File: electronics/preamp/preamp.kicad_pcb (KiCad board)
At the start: 2 copper layers, 25 x 25 mm, 28 parts, among them J1 Conn_01x01, J2 Conn_01x01, J3 Conn_01x05, U1 TL064

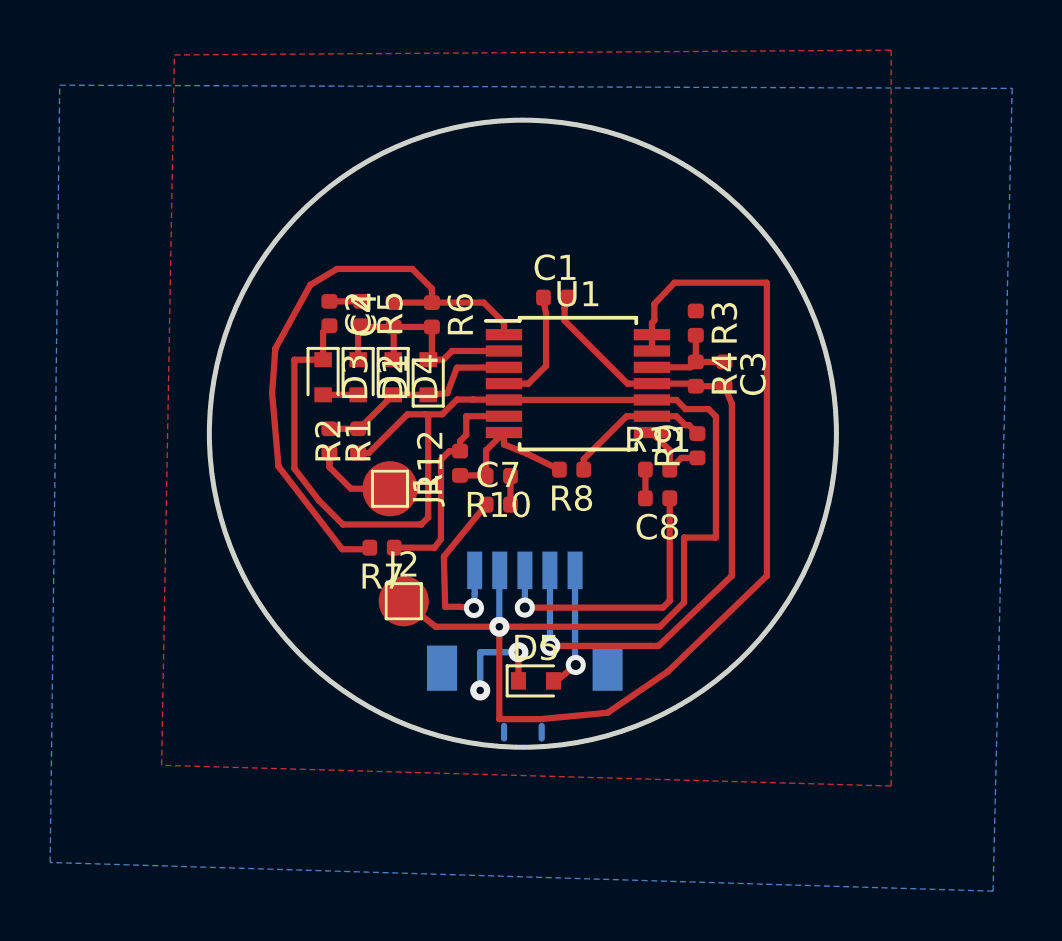
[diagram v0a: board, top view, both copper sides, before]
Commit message: Compress and prettify traces
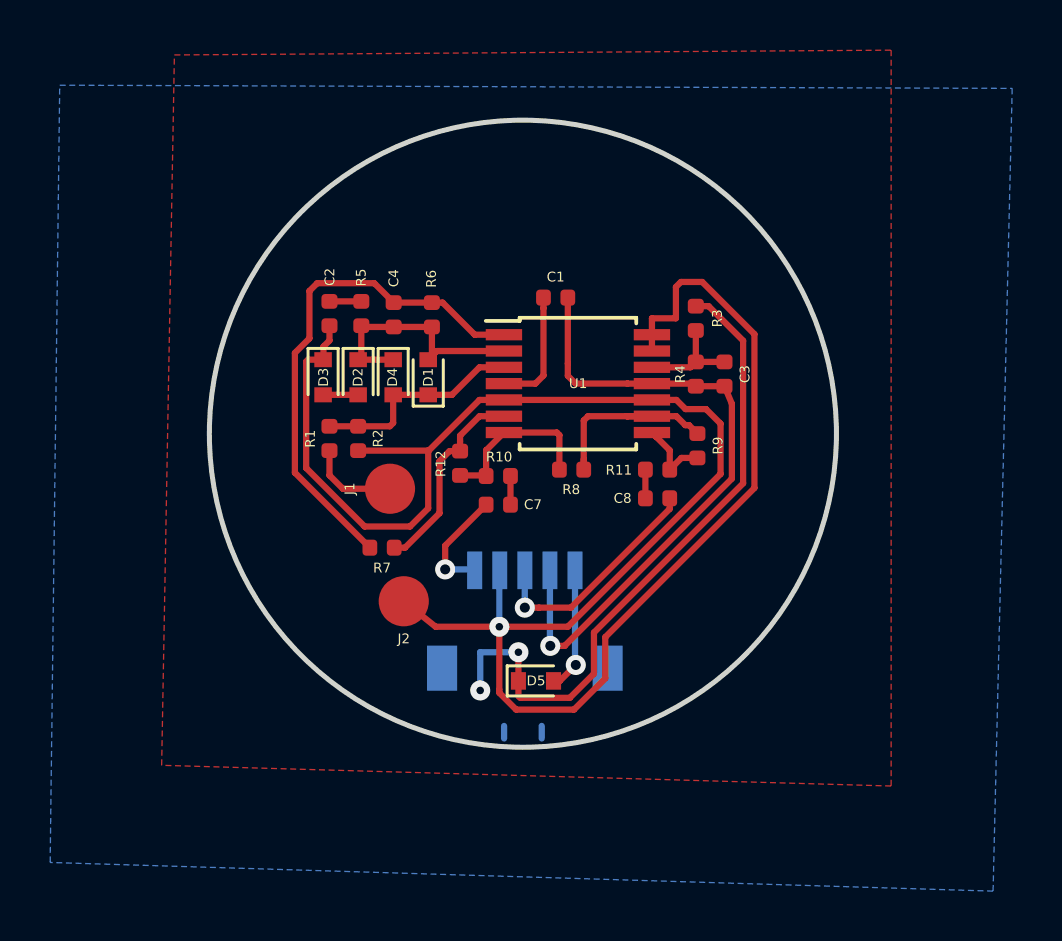
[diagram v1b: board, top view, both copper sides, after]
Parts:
- R9: value 100k 1% -> 100k 1%
- moved R3 0.19 mm to (106.9, 95.4)
- moved R1 0.10 mm to (92.3, 100.2)
- moved R2 0.10 mm to (93.4, 100.2)
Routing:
- net VCC: track 9.00 -> 31.3 mm
- net VGND: track 90.6 -> 81.7 mm
- net /AMP: track 24.0 -> 20.6 mm
- net /OUT+: track 7.38 -> 4.45 mm
- net /INV-: track 5.95 -> 8.28 mm
- net /OUT-: track 11.5 -> 9.32 mm
- net -BATT: track 27.6 -> 26.4 mm
- net /GAIN-: track 9.10 -> 8.12 mm
- net /BUF+: track 5.98 -> 6.71 mm
- net /IN+: track 4.08 -> 3.52 mm

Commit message: preamp: Use via shield
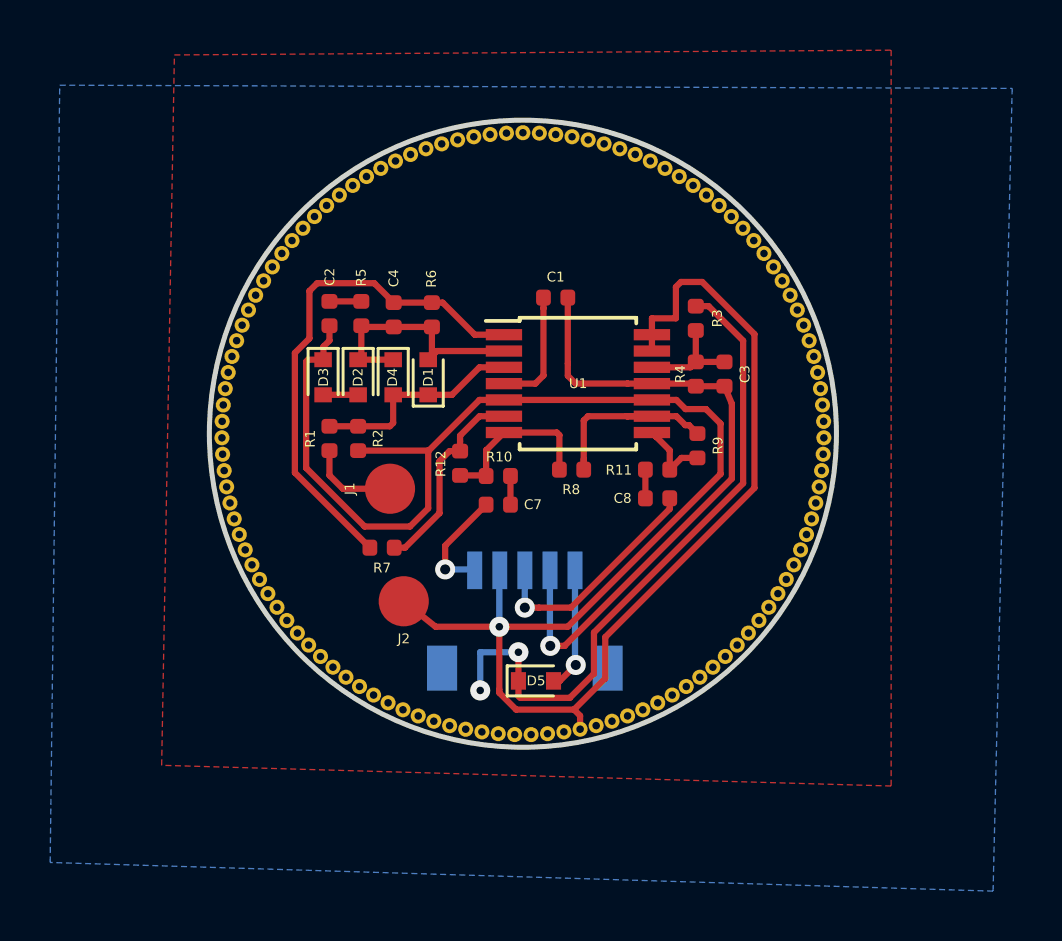
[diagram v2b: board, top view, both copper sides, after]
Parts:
- added J4: Conn_01x01, piezopro:viashield, B.Cu at (100.0, 100.0)
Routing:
- net (no net): track 1.00 -> 0.00 mm
- net VGND: track 81.7 -> 82.6 mm

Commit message: preamp: Move last via underneath connector
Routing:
- net /OUT+: track 4.45 -> 7.40 mm
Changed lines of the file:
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@@
     (thickness 1.6)
     (drawings 65)
-    (tracks 179)
+    (tracks 182)
     (zones 0)
     (modules 29)
@@
   (segment (start 102.280769 111.243357) (end 102.280769 111.78126) (width 0.25) (layer F.Cu) (net 3))
   (segment (start 102.037412 111) (end 102.280769 111.243357) (width 0.25) (layer F.Cu) (net 3))
-  (via (at 96.901 105.41) (size 0.8) (drill 0.4) (layers F.Cu B.Cu) (net 4))
+  (via (at 98.044 106.934) (size 0.8) (drill 0.4) (layers F.Cu B.Cu) (net 4))
   (segment (start 98.041 105.41) (end 98.078 105.447) (width 0.25) (layer B.Cu) (net 4))
-  (segment (start 96.901 105.41) (end 98.041 105.41) (width 0.25) (layer B.Cu) (net 4))
-  (segment (start 96.901 104.46272) (end 96.901 105.41) (width 0.25) (layer F.Cu) (net 4))
   (segment (start 98.53436 102.82936) (end 96.901 104.46272) (width 0.25) (layer F.Cu) (net 4))
+  (segment (start 98.044 106.934) (end 97.028 106.934) (width 0.25) (layer F.Cu) (net 4))
+  (segment (start 96.901 106.807) (end 97.028 106.934) (width 0.25) (layer F.Cu) (net 4))
+  (segment (start 96.901 104.46272) (end 96.901 106.807) (width 0.25) (layer F.Cu) (net 4))
+  (segment (start 98.044 105.481) (end 98.078 105.447) (width 0.25) (layer B.Cu) (net 4))
+  (segment (start 98.044 106.934) (end 98.044 105.481) (width 0.25) (layer B.Cu) (net 4))
   (segment (start 99.50436 101.68636) (end 99.50436 102.82936) (width 0.25) (layer F.Cu) (net 5))
   (segment (start 104.88436 101.43236) (end 104.88436 102.57536) (width 0.25) (layer F.Cu) (net 6))
@@
   )
   (zone (net 3) (net_name VGND) (layer B.Cu) (hatch edge 0.508)
-    (connect_pads (clearance -0.2))
+    (connect_pads yes (clearance -0.2))
     (min_thickness 0.2)
     (fill yes (arc_segments 16) (thermal_gap 0.508) (thermal_bridge_width 0.508))
